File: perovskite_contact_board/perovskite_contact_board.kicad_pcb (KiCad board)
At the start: 2 copper layers, 57 x 52.2 mm, 14 parts, among them J1 Conn_01x08, J2 Conn_01x08, J3 Conn_01x08, J4 Conn_01x08, J5 Conn_01x08, J6 Conn_01x08, U1 Perovskite_CP_6_Cell, U2 Perovskite_CP_6_Cell, U3 Perovskite_CP_6_Cell, U4 MCP9808_MSOP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

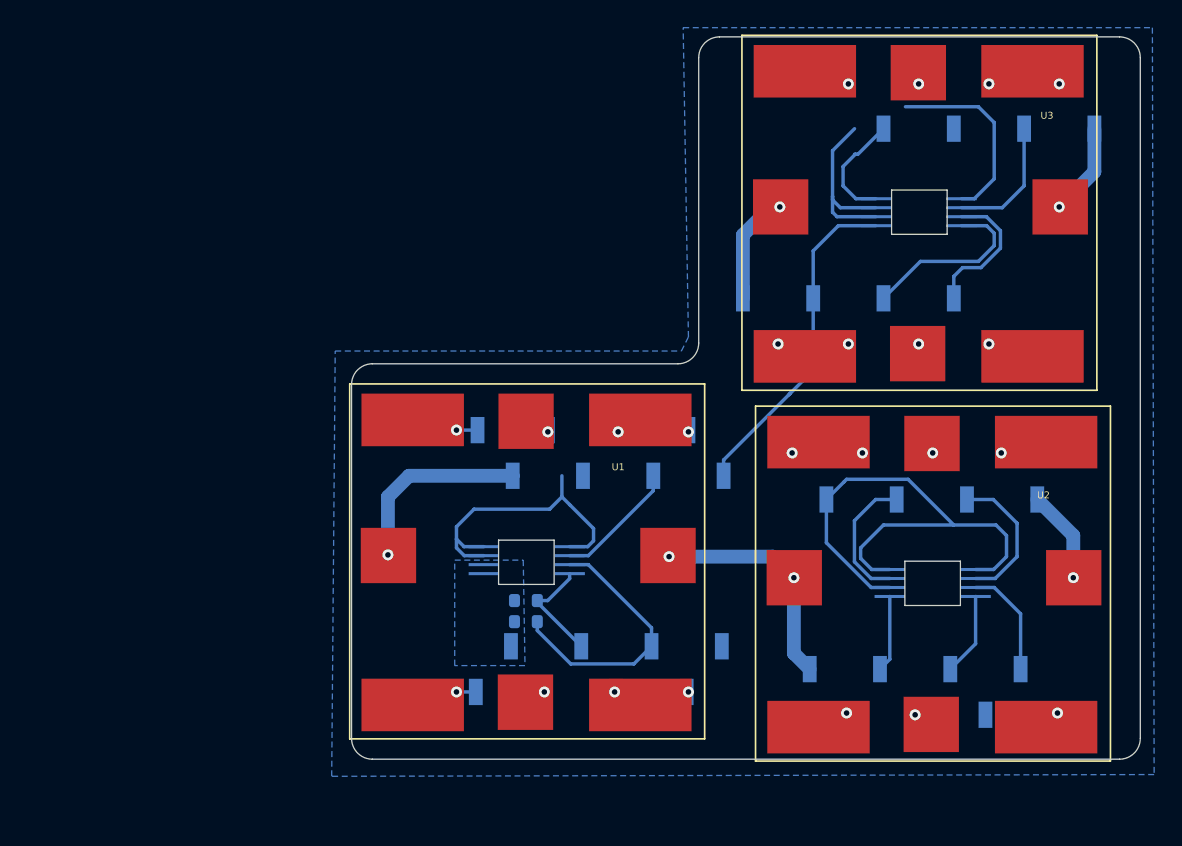
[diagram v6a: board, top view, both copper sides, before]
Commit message: contact board oriented correctly
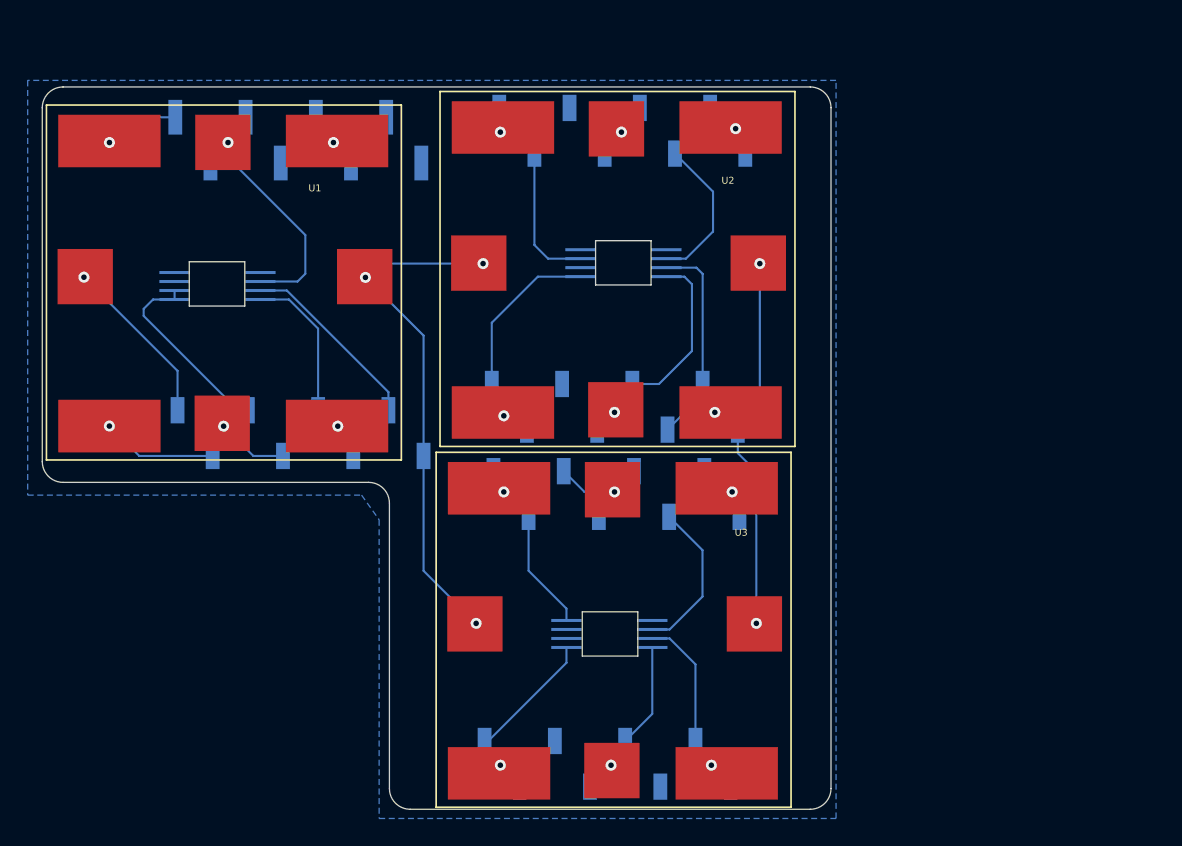
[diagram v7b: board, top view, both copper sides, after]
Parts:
- removed R1, R4: R, Resistor_SMD:R_0603_1608Metric
- J2: footprint Connector_PinSocket_2.54mm:PinSocket_1x08_P2.54mm_Vertical_SMD_Pin1Right -> Connector_PinHeader_2.54mm:PinHeader_1x08_P2.54mm_Vertical_SMD_Pin1Left
- moved J5 54.3 mm to (190.5, 97.7)
- moved J3 46.3 mm to (191.6, 51.9)
- moved J2 44.0 mm to (168.1, 52.6)
- moved U6 37.8 mm to (190.6, 88.3)
- moved U3 37.4 mm to (178.1, 75.1)
- moved U2 32.2 mm to (178.4, 49.1)
- moved U5 32.2 mm to (191.6, 61.5)
- moved U4 29.9 mm to (162.3, 63.1)
- moved U1 29.8 mm to (149.9, 50.0)
- moved J4 22.2 mm to (191.0, 71.8)
- moved J6 21.9 mm to (191.1, 78.2)
- moved J1 21.7 mm to (168.3, 73.8), turned to 270 degrees
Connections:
- J1 pad 1: VDD -> CP
- J1 pad 2: CELL_3 -> CELL_6
- J1 pad 3: ALERT1 -> VDD
- J1 pad 4: CELL_3 -> CELL_5
- J1 pad 5: GND -> SDA
- J1 pad 6: CELL_2 -> CELL_4
- J1 pad 7: CP -> SCL
- J1 pad 8: CELL_1 -> CP
- J2 pad 2: CELL_4 -> GND
- J2 pad 3: SCL -> GND
- J2 pad 4: CELL_4 -> CELL_3
- J2 pad 5: SDA -> GND
- J2 pad 6: CELL_5 -> CELL_2
- J2 pad 7: VDD -> ALERT1
- J2 pad 8: CELL_6 -> CELL_1
- J3 pad 1: CELL_10 -> GND
- J3 pad 2: SCL -> CELL_9
- J3 pad 3: (no net) -> ALERT2
- J3 pad 4: SDA -> CELL_8
- J3 pad 5: CELL_11 -> GND
- J3 pad 6: VDD -> GND
- J3 pad 7: CELL_12 -> VDD
- J3 pad 8: CP -> CELL_7
- J4 pad 2: CELL_9 -> SCL
- J4 pad 3: ALERT2 -> CELL_10
- J4 pad 4: CELL_8 -> SDA
- J4 pad 5: VDD -> CELL_11
- J4 pad 6: CELL_7 -> GND
- J4 pad 7: GND -> CELL_12
- J4 pad 8: CELL_7 -> VDD
- J5 pad 1: CP -> CELL_16
- J5 pad 2: CELL_15 -> SCL
- J5 pad 3: ALERT3 -> GND
- J5 pad 4: CELL_15 -> SDA
- J5 pad 5: GND -> CELL_17
- J5 pad 6: CELL_14 -> GND
- J5 pad 7: VDD -> CELL_18
- J5 pad 8: CELL_13 -> VDD
- J6 pad 1: CELL_16 -> GND
- J6 pad 2: SCL -> CELL_15
- J6 pad 3: CELL_17 -> ALERT3
- J6 pad 4: SDA -> GND
- J6 pad 5: CELL_18 -> GND
- J6 pad 6: VDD -> CELL_14
- J6 pad 7: CELL_18 -> VDD
- J6 pad 8: CP -> CELL_13
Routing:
- net GND: track 88.6 -> 0.00 mm
- net CP: track 52.1 -> 77.4 mm
- net CELL_6: track 1.40 -> 8.36 mm
- net VDD: track 47.8 -> 54.6 mm
- net ALERT1: track 9.07 -> 15.7 mm
- net CELL_5: track 0.00 -> 5.18 mm
- net CELL_14: track 0.00 -> 4.29 mm
- net SCL: track 37.9 -> 33.8 mm
- net CELL_1: track 1.52 -> 5.51 mm
- net CELL_10: track 0.00 -> 3.94 mm
- net SDA: track 27.0 -> 30.7 mm
- net CELL_15: track 0.00 -> 2.63 mm, vias 2 -> 1
- net CELL_4: track 0.00 -> 2.61 mm, vias 2 -> 1
- net CELL_9: track 0.00 -> 2.46 mm
- net CELL_3: track 0.00 -> 2.35 mm, vias 2 -> 1
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- removed copper zone on B.Cu, net +5V
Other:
- outline, holes or cut-outs redrawn
